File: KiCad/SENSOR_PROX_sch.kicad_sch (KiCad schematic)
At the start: 1 part, among them U6 VL53L1CXV0FY1

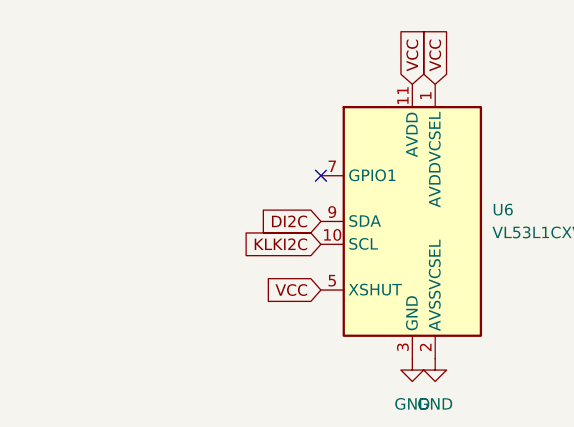
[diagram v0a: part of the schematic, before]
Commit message: reducido motores y finales de carrera
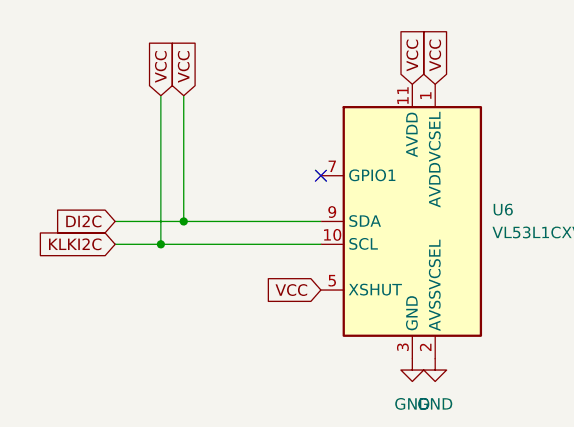
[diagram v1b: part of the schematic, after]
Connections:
- net KLKI2C is gone; now on net DI2C: U6.10 (SCL)
- net VCC is gone; now on net DI2C: U6.1 (AVDDVCSEL), U6.11 (AVDD), U6.5 (XSHUT)
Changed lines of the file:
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@@
 	(generator_version "9.0")
 	(paper "A4")
+	(junction
+		(at 129.54 71.12)
+		(diameter 0)
+		(color 0 0 0 0)
+	)
+	(junction
+		(at 127 73.66)
+		(diameter 0)
+		(color 0 0 0 0)
+	)
 	(no_connect
 		(at 144.78 66.04)
 	)
+	(wire
+		(pts
+			(xy 127 73.66) (xy 144.78 73.66)
+		)
+		(stroke
+			(width 0)
+			(type default)
+		)
+	)
+	(wire
+		(pts
+			(xy 129.54 57.15) (xy 129.54 71.12)
+		)
+		(stroke
+			(width 0)
+			(type default)
+		)
+	)
+	(wire
+		(pts
+			(xy 129.54 71.12) (xy 144.78 71.12)
+		)
+		(stroke
+			(width 0)
+			(type default)
+		)
+	)
+	(wire
+		(pts
+			(xy 127 57.15) (xy 127 73.66)
+		)
+		(stroke
+			(width 0)
+			(type default)
+		)
+	)
+	(wire
+		(pts
+			(xy 121.92 73.66) (xy 127 73.66)
+		)
+		(stroke
+			(width 0)
+			(type default)
+		)
+	)
+	(wire
+		(pts
+			(xy 121.92 71.12) (xy 129.54 71.12)
+		)
+		(stroke
+			(width 0)
+			(type default)
+		)
+	)
 	(global_label "KLKI2C"
 		(shape input)
-		(at 144.78 73.66 180)
+		(at 121.92 73.66 180)
 		(fields_autoplaced yes)
 		(effects
@@
 		)
 		(property "Intersheetrefs" "${INTERSHEET_REFS}"
-			(at 135.1424 73.66 0)
+			(at 112.2824 73.66 0)
 			(effects
 				(font
@@
 		)
 	)
+	(global_label "VCC"
+		(shape input)
+		(at 129.54 57.15 90)
+		(fields_autoplaced yes)
+		(effects
+			(font
+				(size 1.27 1.27)
+			)
+			(justify left)
+		)
+		(property "Intersheetrefs" "${INTERSHEET_REFS}"
+			(at 129.54 50.5362 90)
+			(effects
+				(font
+					(size 1.27 1.27)
+				)
+				(justify left)
+				(hide yes)
+			)
+		)
+	)
 	(global_label "DI2C"
 		(shape input)
-		(at 144.78 71.12 180)
+		(at 121.92 71.12 180)
 		(fields_autoplaced yes)
 		(effects
@@
 		)
 		(property "Intersheetrefs" "${INTERSHEET_REFS}"
-			(at 137.4405 71.12 0)
+			(at 114.5805 71.12 0)
 			(effects
 				(font
@@
 				(hide yes)
 			)
+		)
+	)
+	(global_label "VCC"
+		(shape input)
+		(at 127 57.15 90)
+		(fields_autoplaced yes)
+		(effects
+			(font
+				(size 1.27 1.27)
+			)
+			(justify left)
+		)
+		(property "Intersheetrefs" "${INTERSHEET_REFS}"
+			(at 127 50.5362 90)
+			(effects
+				(font
+					(size 1.27 1.27)
+				)
+				(justify left)
+				(hide yes)
+			)

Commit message: he añadido huelas a algunos componentes importates
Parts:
- added R8, R9: R, symbol Device:R
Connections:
- net DI2C: now also R8.2; no longer U6.1 (AVDDVCSEL), U6.10 (SCL), U6.11 (AVDD), U6.5 (XSHUT)
- new net KLKI2C: R9.2, U6.10 (SCL)
- new net VCC: R8.1, R9.1, U6.1 (AVDDVCSEL), U6.11 (AVDD), U6.5 (XSHUT)
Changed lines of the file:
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@@
 	(paper "A4")
 	(junction
-		(at 129.54 71.12)
+		(at 127 71.12)
 		(diameter 0)
 		(color 0 0 0 0)
 	)
 	(junction
-		(at 127 73.66)
+		(at 129.54 73.66)
 		(diameter 0)
 		(color 0 0 0 0)
@@
 	(wire
 		(pts
-			(xy 127 73.66) (xy 144.78 73.66)
+			(xy 121.92 73.66) (xy 129.54 73.66)
 		)
 		(stroke
@@
 	(wire
 		(pts
-			(xy 129.54 57.15) (xy 129.54 71.12)
+			(xy 129.54 64.77) (xy 129.54 73.66)
 		)
 		(stroke
@@
 	(wire
 		(pts
-			(xy 129.54 71.12) (xy 144.78 71.12)
+			(xy 127 64.77) (xy 127 71.12)
 		)
 		(stroke
@@
 	(wire
 		(pts
-			(xy 127 57.15) (xy 127 73.66)
+			(xy 127 71.12) (xy 144.78 71.12)
 		)
 		(stroke
@@
 	(wire
 		(pts
-			(xy 121.92 73.66) (xy 127 73.66)
+			(xy 121.92 71.12) (xy 127 71.12)
 		)
 		(stroke
@@
 	(wire
 		(pts
-			(xy 121.92 71.12) (xy 129.54 71.12)
+			(xy 129.54 73.66) (xy 144.78 73.66)
 		)
 		(stroke
@@
 				(justify left)
 				(hide yes)
+			)
+		)
+	)
+	(symbol
+		(lib_id "Device:R")
+		(at 127 60.96 0)
+		(unit 1)
+		(exclude_from_sim no)
+		(in_bom yes)
+		(on_board yes)
+		(dnp no)
+		(fields_autoplaced yes)
+		(property "Reference" "R8"
+			(at 129.54 59.6899 0)
+			(effects
+				(font
+					(size 1.27 1.27)
+				)
+				(justify left)
+			)
+		)
+		(property "Value" "R"
+			(at 129.54 62.2299 0)
+			(effects
+				(font
+					(size 1.27 1.27)
+				)
+				(justify left)
+			)
+		)
+		(property "Footprint" ""
+			(at 125.222 60.96 90)
+			(effects
+				(font
+					(size 1.27 1.27)
+				)
+				(hide yes)
+			)
+		)
+		(property "Datasheet" "~"
+			(at 127 60.96 0)
+			(effects
+				(font
+					(size 1.27 1.27)
+				)
+				(hide yes)
+			)
+		)
+		(property "Description" "Resistor"
+			(at 127 60.96 0)
+			(effects
+				(font
+					(size 1.27 1.27)
+				)
+				(hide yes)
+			)
+		)
+		(pin "1"
+		)
+		(pin "2"
+		)
+		(instances
+			(project "Retrovisores"
+				(path "/9b9f005f-0621-4675-bd4e-683e7082b120/5ac1b284-cf75-4bf4-9e32-45476caa1b97"
+					(reference "R8")
+					(unit 1)
+				)
 			)
 		)
@@
 					(unit 1)
 				)
+			)
+		)
+	)
+	(symbol
+		(lib_id "Device:R")
+		(at 129.54 60.96 0)
+		(unit 1)
+		(exclude_from_sim no)
+		(in_bom yes)
+		(on_board yes)
+		(dnp no)
+		(fields_autoplaced yes)
+		(property "Reference" "R9"
+			(at 132.08 59.6899 0)
+			(effects
+				(font
+					(size 1.27 1.27)
+				)
+				(justify left)
+			)
+		)
+		(property "Value" "R"
+			(at 132.08 62.2299 0)
+			(effects
+				(font
+					(size 1.27 1.27)
+				)
+				(justify left)
+			)
+		)
+		(property "Footprint" ""
+			(at 127.762 60.96 90)
+			(effects
+				(font
+					(size 1.27 1.27)
+				)
+				(hide yes)
+			)
+		)
+		(property "Datasheet" "~"
+			(at 129.54 60.96 0)
+			(effects
+				(font
+					(size 1.27 1.27)
+				)
+				(hide yes)
+			)
+		)
+		(property "Description" "Resistor"
+			(at 129.54 60.96 0)
+			(effects
+				(font
+					(size 1.27 1.27)
+				)
+				(hide yes)
+			)
+		)
+		(pin "1"
+		)
+		(pin "2"
+		)
+		(instances
+			(project "Retrovisores"
+				(path "/9b9f005f-0621-4675-bd4e-683e7082b120/5ac1b284-cf75-4bf4-9e32-45476caa1b97"
+					(reference "R9")
+					(unit 1)
+				)

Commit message: he añadido el resto de huellas, he corregido algunos errores en la parte de alimentación en los diodos. tambien he trasladados todas las huellas a la pcb y lo he intentado separar un poco para verlo mas claro cuando empecemos el placing.
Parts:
- R8, R9: footprint (none) -> Resistor_SMD:R_0402_1005Metric
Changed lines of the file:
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@@
 			)
 		)
-		(property "Footprint" ""
+		(property "Footprint" "Resistor_SMD:R_0402_1005Metric"
 			(at 125.222 60.96 90)
 			(effects
@@
 			)
 		)
-		(property "Footprint" ""
+		(property "Footprint" "Resistor_SMD:R_0402_1005Metric"
 			(at 127.762 60.96 90)
 			(effects

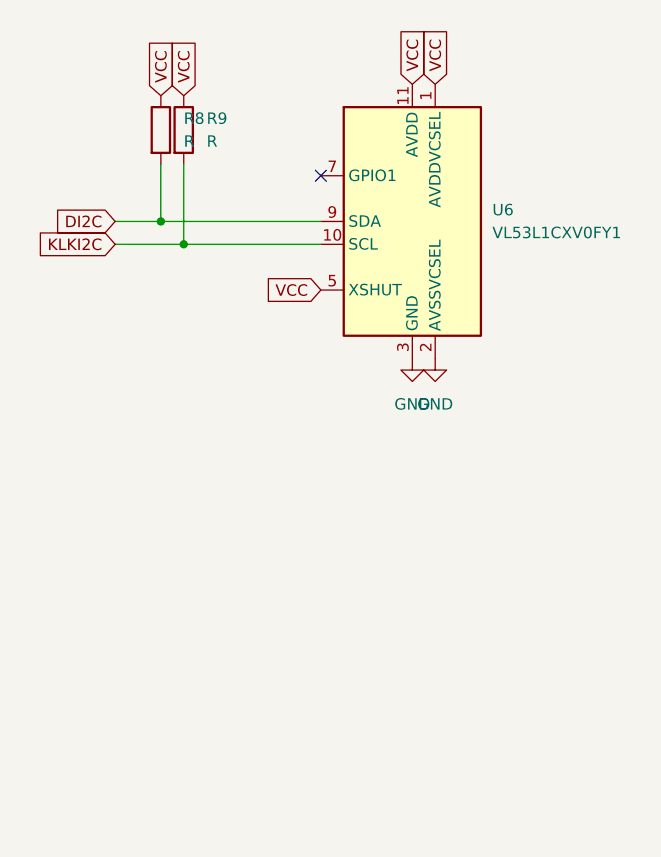
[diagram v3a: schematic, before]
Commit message: terminado placement (reorganizado pines del micro y añadido cambios de sensores/calefactor por conectores)
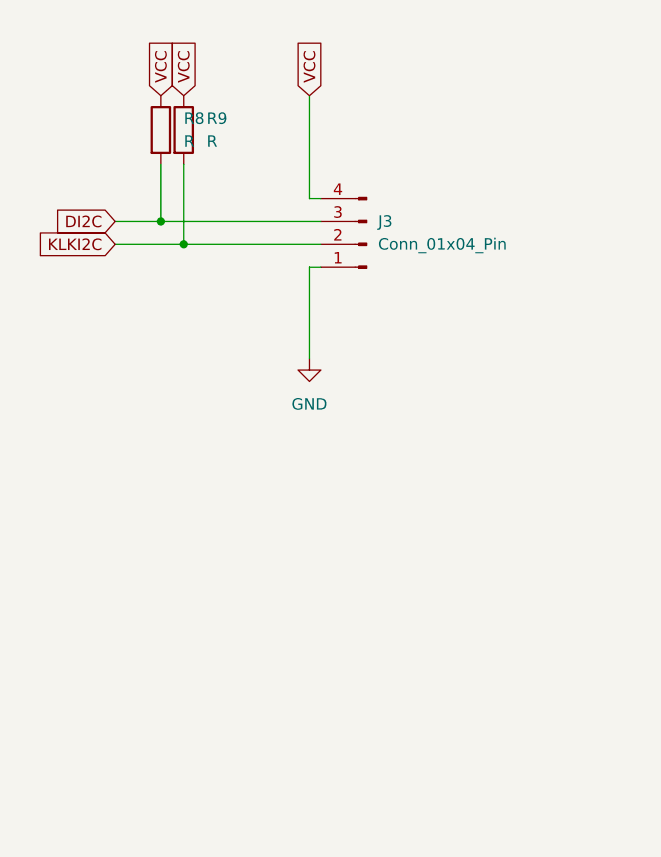
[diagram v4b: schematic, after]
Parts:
- removed U6: VL53L1CXV0FY1, Sensor_Distance:ST_VL53L1x, symbol Sensor_Distance:VL53L1CXV0FY1
- added J3: Conn_01x04_Pin, Connector_PinHeader_2.54mm:PinHeader_1x04_P2.54mm_Vertical, symbol Connector:Conn_01x04_Pin
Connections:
- net DI2C: now also J3.3 (Pin_3)
- net GND: now also J3.1 (Pin_1)
- net KLKI2C: now also J3.2 (Pin_2)
- net VCC: now also J3.4 (Pin_4)
- no-connect marks 1 -> 0
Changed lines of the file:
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@@
 		(color 0 0 0 0)
 	)
-	(no_connect
-		(at 144.78 66.04)
-	)
 	(wire
 		(pts
@@
 	(wire
 		(pts
+			(xy 143.51 68.58) (xy 144.78 68.58)
+		)
+		(stroke
+			(width 0)
+			(type default)
+		)
+	)
+	(wire
+		(pts
+			(xy 143.51 86.36) (xy 143.51 76.2)
+		)
+		(stroke
+			(width 0)
+			(type default)
+		)
+	)
+	(wire
+		(pts
 			(xy 127 71.12) (xy 144.78 71.12)
 		)
@@
 		)
 	)
+	(wire
+		(pts
+			(xy 143.51 76.2) (xy 144.78 76.2)
+		)
+		(stroke
+			(width 0)
+			(type default)
+		)
+	)
+	(wire
+		(pts
+			(xy 143.51 57.15) (xy 143.51 68.58)
+		)
+		(stroke
+			(width 0)
+			(type default)
+		)
+	)
 	(global_label "KLKI2C"
 		(shape input)
@@
 	(global_label "VCC"
 		(shape input)
-		(at 154.94 55.88 90)
+		(at 143.51 57.15 90)
 		(fields_autoplaced yes)
 		(effects
@@
 		)
 		(property "Intersheetrefs" "${INTERSHEET_REFS}"
-			(at 154.94 49.2662 90)
-			(effects
-				(font
-					(size 1.27 1.27)
-				)
-				(justify left)
-				(hide yes)
-			)
-		)
-	)
-	(global_label "VCC"
-		(shape input)
-		(at 157.48 55.88 90)
-		(fields_autoplaced yes)
-		(effects
-			(font
-				(size 1.27 1.27)
-			)
-			(justify left)
-		)
-		(property "Intersheetrefs" "${INTERSHEET_REFS}"
-			(at 157.48 49.2662 90)
-			(effects
-				(font
-					(size 1.27 1.27)
-				)
-				(justify left)
-				(hide yes)
-			)
-		)
-	)
-	(global_label "VCC"
-		(shape input)
-		(at 144.78 78.74 180)
-		(fields_autoplaced yes)
-		(effects
-			(font
-				(size 1.27 1.27)
-			)
-			(justify right)
-		)
-		(property "Intersheetrefs" "${INTERSHEET_REFS}"
-			(at 138.1662 78.74 0)
-			(effects
-				(font
-					(size 1.27 1.27)
-				)
-				(justify right)
+			(at 143.51 50.5362 90)
+			(effects
+				(font
+					(size 1.27 1.27)
+				)
+				(justify left)
 				(hide yes)
 			)
@@
 	(symbol
 		(lib_id "power:GND")
-		(at 157.48 86.36 0)
+		(at 143.51 86.36 0)
 		(unit 1)
 		(exclude_from_sim no)
@@
 		(fields_autoplaced yes)
 		(property "Reference" "#PWR019"
-			(at 157.48 92.71 0)
+			(at 143.51 92.71 0)
 			(effects
 				(font
@@
 		)
 		(property "Value" "GND"
-			(at 157.48 91.44 0)
+			(at 143.51 91.44 0)
 			(effects
 				(font
@@
 		)
 		(property "Footprint" ""
-			(at 157.48 86.36 0)
+			(at 143.51 86.36 0)
 			(effects
 				(font
@@
 		)
 		(property "Datasheet" ""
-			(at 157.48 86.36 0)
+			(at 143.51 86.36 0)
 			(effects
 				(font
@@
 		)
 		(property "Description" "Power symbol creates a global label with name \"GND\" , ground"
-			(at 157.48 86.36 0)
+			(at 143.51 86.36 0)
 			(effects
 				(font
@@
 	)
 	(symbol
-		(lib_id "Sensor_Distance:VL53L1CXV0FY1")
-		(at 154.94 71.12 0)
+		(lib_id "Connector:Conn_01x04_Pin")
+		(at 149.86 73.66 180)
 		(unit 1)
 		(exclude_from_sim no)
@@
 		(dnp no)
 		(fields_autoplaced yes)
-		(property "Reference" "U6"
-			(at 163.83 69.8499 0)
-			(effects
-				(font
-					(size 1.27 1.27)
-				)
-				(justify left)
-			)
-		)
-		(property "Value" "VL53L1CXV0FY1"
-			(at 163.83 72.3899 0)
-			(effects
-				(font
-					(size 1.27 1.27)
-				)
-				(justify left)
-			)
-		)
-		(property "Footprint" "Sensor_Distance:ST_VL53L1x"
-			(at 172.085 85.09 0)
-			(effects
-				(font
-					(size 1.27 1.27)
-				)
-				(hide yes)
-			)
-		)
-		(property "Datasheet" "https://www.st.com/resource/en/datasheet/vl53l1x.pdf"
-			(at 157.48 71.12 0)
-			(effects
-				(font
-					(size 1.27 1.27)
-				)
-				(hide yes)
-			)
-		)
-		(property "Description" "4m distance ranging ToF sensor, Optical LGA12"
-			(at 154.94 71.12 0)
-			(effects
-				(font
-					(size 1.27 1.27)
-				)
-				(hide yes)
-			)
+		(property "Reference" "J3"
+			(at 151.13 71.1199 0)
+			(effects
+				(font
+					(size 1.27 1.27)
+				)
+				(justify right)
+			)
+		)
+		(property "Value" "Conn_01x04_Pin"
+			(at 151.13 73.6599 0)
+			(effects
+				(font
+					(size 1.27 1.27)
+				)
+				(justify right)
+			)
+		)
+		(property "Footprint" "Connector_PinHeader_2.54mm:PinHeader_1x04_P2.54mm_Vertical"
+			(at 149.86 73.66 0)
+			(effects
+				(font
+					(size 1.27 1.27)
+				)
+				(hide yes)
+			)
+		)
+		(property "Datasheet" "~"
+			(at 149.86 73.66 0)
+			(effects
+				(font
+					(size 1.27 1.27)
+				)
+				(hide yes)
+			)
+		)
+		(property "Description" "Generic connector, single row, 01x04, script generated"
+			(at 149.86 73.66 0)
+			(effects
+				(font
+					(size 1.27 1.27)
+				)
+				(hide yes)
+			)
+		)
+		(pin "4"
 		)
 		(pin "1"
 		)
-		(pin "5"
-		)
-		(pin "11"
+		(pin "2"
 		)
 		(pin "3"
 		)
-		(pin "10"
-		)
-		(pin "8"
-		)
-		(pin "4"
-		)
-		(pin "6"
-		)
-		(pin "2"
-		)
-		(pin "12"
-		)
-		(pin "9"
-		)
-		(pin "7"
-		)
 		(instances
-			(project "Retrovisores"
+			(project ""
 				(path "/9b9f005f-0621-4675-bd4e-683e7082b120/5ac1b284-cf75-4bf4-9e32-45476caa1b97"
-					(reference "U6")
+					(reference "J3")
 					(unit 1)
 				)
-			)
-		)
-	)
-	(symbol
-		(lib_id "power:GND")
-		(at 154.94 86.36 0)
-		(unit 1)
-		(exclude_from_sim no)
-		(in_bom yes)
-		(on_board yes)
-		(dnp no)
-		(fields_autoplaced yes)
-		(property "Reference" "#PWR018"
-			(at 154.94 92.71 0)
-			(effects
-				(font
-					(size 1.27 1.27)
-				)
-				(hide yes)
-			)
-		)
-		(property "Value" "GND"
-			(at 154.94 91.44 0)
-			(effects
-				(font
-					(size 1.27 1.27)
-				)
-			)
-		)
-		(property "Footprint" ""
-			(at 154.94 86.36 0)
-			(effects
-				(font
-					(size 1.27 1.27)
-				)
-				(hide yes)
-			)
-		)
-		(property "Datasheet" ""
-			(at 154.94 86.36 0)
-			(effects
-				(font
-					(size 1.27 1.27)
-				)
-				(hide yes)
-			)
-		)
-		(property "Description" "Power symbol creates a global label with name \"GND\" , ground"
-			(at 154.94 86.36 0)
-			(effects
-				(font
-					(size 1.27 1.27)
-				)
-				(hide yes)
-			)
-		)
-		(pin "1"
-		)
-		(instances
-			(project "Retrovisores"
-				(path "/9b9f005f-0621-4675-bd4e-683e7082b120/5ac1b284-cf75-4bf4-9e32-45476caa1b97"
-					(reference "#PWR018")
-					(unit 1)
-				)

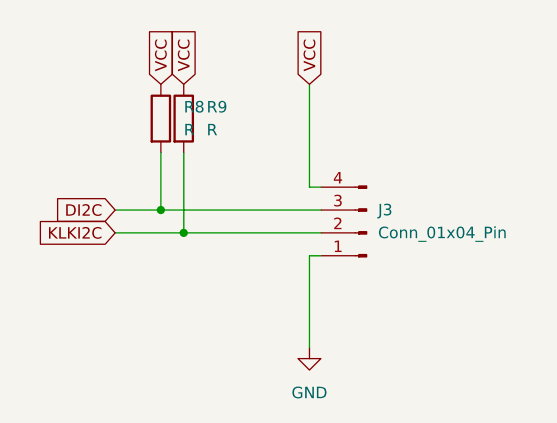
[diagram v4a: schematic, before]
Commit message: añadido test points y solucionado un error con gnd en alimentación
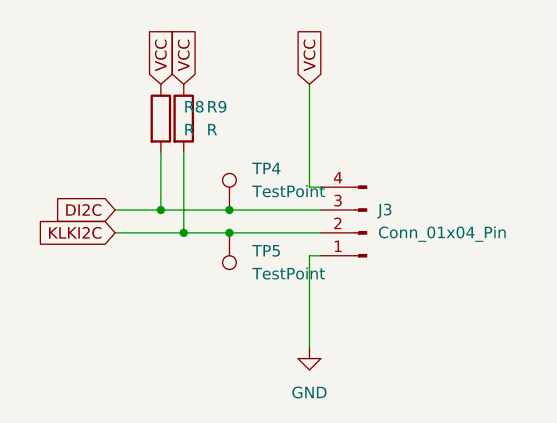
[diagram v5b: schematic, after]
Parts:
- added TP4, TP5: TestPoint, TestPoint:TestPoint_Bridge_Pitch2.0mm_Drill0.7mm, symbol Connector:TestPoint
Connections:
- net DI2C: now also TP4.1
- net KLKI2C: now also TP5.1
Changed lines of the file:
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@@
+	)
+	(junction
+		(at 134.62 73.66)
+		(diameter 0)
+		(color 0 0 0 0)
+	)
+	(junction
+		(at 134.62 71.12)
+		(diameter 0)
+		(color 0 0 0 0)
 	)
 	(junction
@@
 	(wire
 		(pts
-			(xy 127 71.12) (xy 144.78 71.12)
+			(xy 134.62 73.66) (xy 144.78 73.66)
+		)
+		(stroke
+			(width 0)
+			(type default)
+		)
+	)
+	(wire
+		(pts
+			(xy 127 71.12) (xy 134.62 71.12)
 		)
 		(stroke
@@
 	(wire
 		(pts
-			(xy 129.54 73.66) (xy 144.78 73.66)
+			(xy 134.62 71.12) (xy 144.78 71.12)
+		)
+		(stroke
+			(width 0)
+			(type default)
+		)
+	)
+	(wire
+		(pts
+			(xy 129.54 73.66) (xy 134.62 73.66)
 		)
 		(stroke
@@
 					(unit 1)
 				)
+			)
+		)
+	)
+	(symbol
+		(lib_id "Connector:TestPoint")
+		(at 134.62 71.12 0)
+		(unit 1)
+		(exclude_from_sim no)
+		(in_bom yes)
+		(on_board yes)
+		(dnp no)
+		(fields_autoplaced yes)
+		(property "Reference" "TP4"
+			(at 137.16 66.5479 0)
+			(effects
+				(font
+					(size 1.27 1.27)
+				)
+				(justify left)
+			)
+		)
+		(property "Value" "TestPoint"
+			(at 137.16 69.0879 0)
+			(effects
+				(font
+					(size 1.27 1.27)
+				)
+				(justify left)
+			)
+		)
+		(property "Footprint" "TestPoint:TestPoint_Bridge_Pitch2.0mm_Drill0.7mm"
+			(at 139.7 71.12 0)
+			(effects
+				(font
+					(size 1.27 1.27)
+				)
+				(hide yes)
+			)
+		)
+		(property "Datasheet" "~"
+			(at 139.7 71.12 0)
+			(effects
+				(font
+					(size 1.27 1.27)
+				)
+				(hide yes)
+			)
+		)
+		(property "Description" "test point"
+			(at 134.62 71.12 0)
+			(effects
+				(font
+					(size 1.27 1.27)
+				)
+				(hide yes)
+			)
+		)
+		(pin "1"
+		)
+		(instances
+			(project "Retrovisores"
+				(path "/9b9f005f-0621-4675-bd4e-683e7082b120/5ac1b284-cf75-4bf4-9e32-45476caa1b97"
+					(reference "TP4")
+					(unit 1)
+				)
+			)
+		)
+	)
+	(symbol
+		(lib_id "Connector:TestPoint")
+		(at 134.62 73.66 180)
+		(unit 1)
+		(exclude_from_sim no)
+		(in_bom yes)
+		(on_board yes)
+		(dnp no)
+		(fields_autoplaced yes)
+		(property "Reference" "TP5"
+			(at 137.16 75.6919 0)
+			(effects
+				(font
+					(size 1.27 1.27)
+				)
+				(justify right)
+			)
+		)
+		(property "Value" "TestPoint"
+			(at 137.16 78.2319 0)
+			(effects
+				(font
+					(size 1.27 1.27)
+				)
+				(justify right)
+			)
+		)
+		(property "Footprint" "TestPoint:TestPoint_Bridge_Pitch2.0mm_Drill0.7mm"
+			(at 129.54 73.66 0)
+			(effects
+				(font
+					(size 1.27 1.27)
+				)
+				(hide yes)
+			)
+		)
+		(property "Datasheet" "~"
+			(at 129.54 73.66 0)
+			(effects
+				(font
+					(size 1.27 1.27)
+				)
+				(hide yes)
+			)
+		)
+		(property "Description" "test point"
+			(at 134.62 73.66 0)
+			(effects
+				(font
+					(size 1.27 1.27)
+				)
+				(hide yes)
+			)
+		)
+		(pin "1"
+		)
+		(instances
+			(project "Retrovisores"
+				(path "/9b9f005f-0621-4675-bd4e-683e7082b120/5ac1b284-cf75-4bf4-9e32-45476caa1b97"
+					(reference "TP5")
+					(unit 1)
+				)

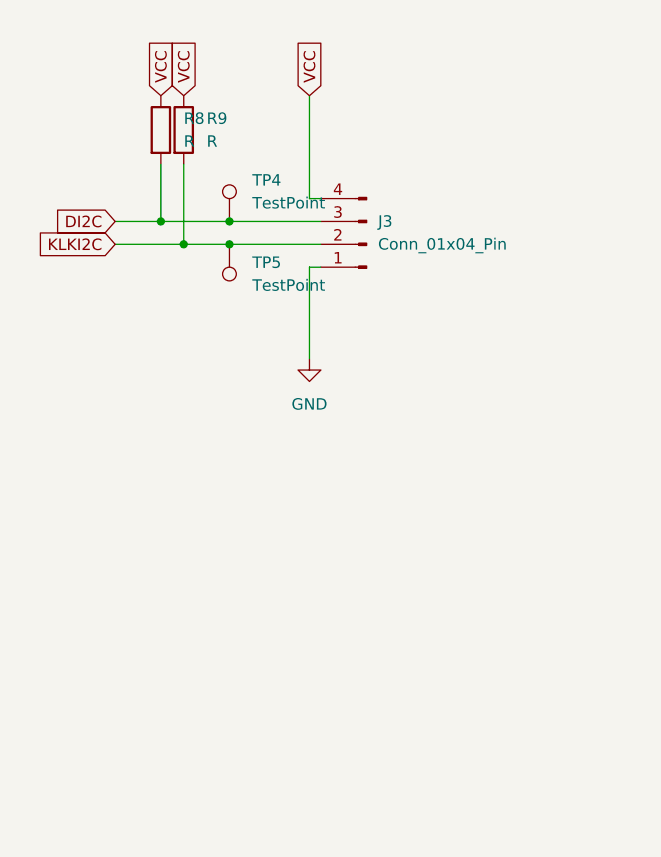
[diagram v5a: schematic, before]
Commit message: reorganizado el esquematico
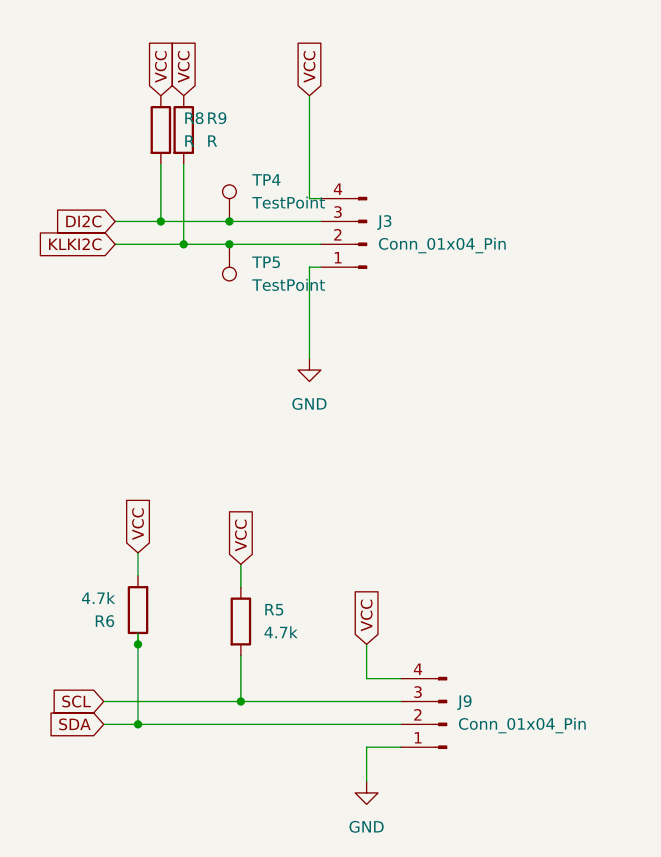
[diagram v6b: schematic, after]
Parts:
- added J9: Conn_01x04_Pin, Connector_PinHeader_2.54mm:PinHeader_1x04_P2.54mm_Vertical, symbol Connector:Conn_01x04_Pin
- added R5, R6: 4.7k, Resistor_SMD:R_0402_1005Metric, symbol Device:R
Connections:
- net GND: now also J9.1 (Pin_1)
- net VCC: now also J9.4 (Pin_4), R5.1, R6.2
- new net SCL: J9.3 (Pin_3), R5.2
- new net SDA: J9.2 (Pin_2), R6.1
